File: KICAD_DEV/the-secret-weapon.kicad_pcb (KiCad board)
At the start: 6 copper layers, 100 x 100 mm, 45 parts, among them J1 USB_C_Receptacle_USB2.0_14P, J2 Screw_Terminal_01x02, U1 STM32H743VITx, U2 USBLC6-2SC6, U3 LMR33640ADDA, U4 LM1086S-3.3/TR, Y1 8 MHz, Y2 32.768 KHz

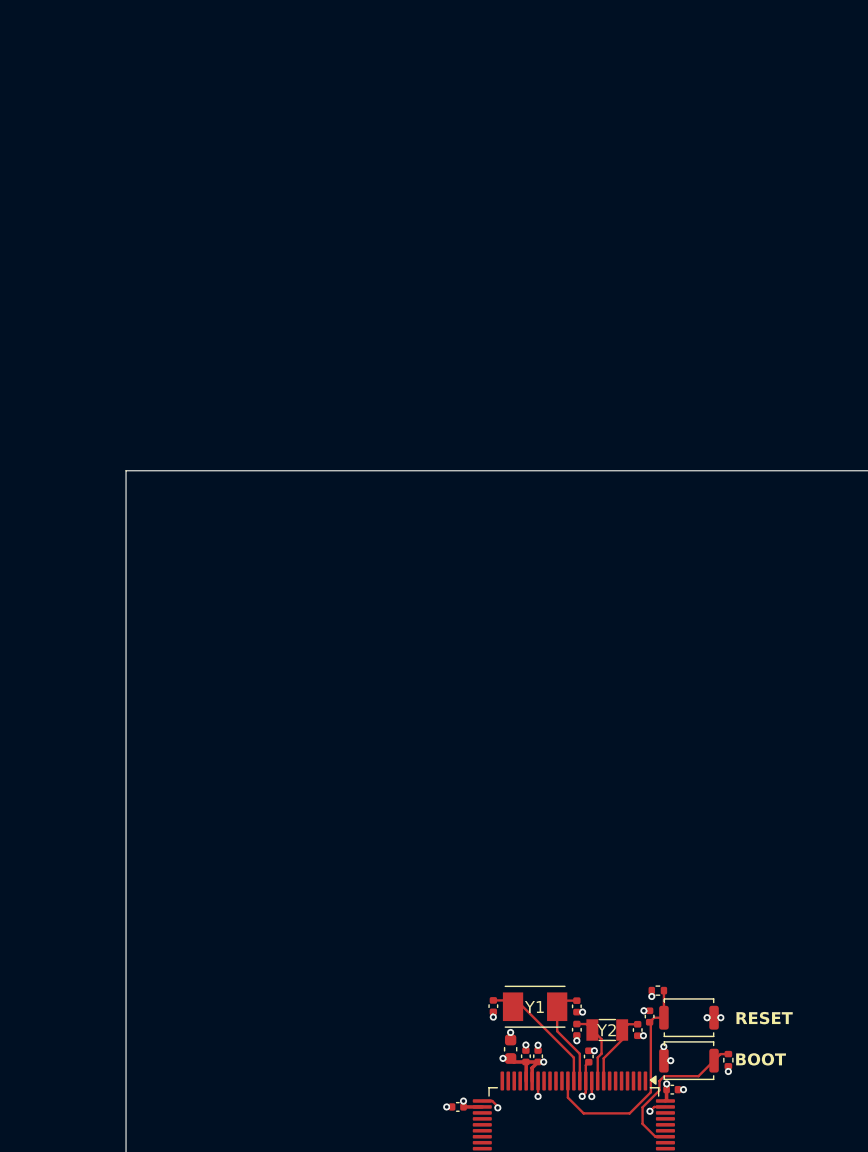
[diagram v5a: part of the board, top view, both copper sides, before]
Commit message: layed out all the components
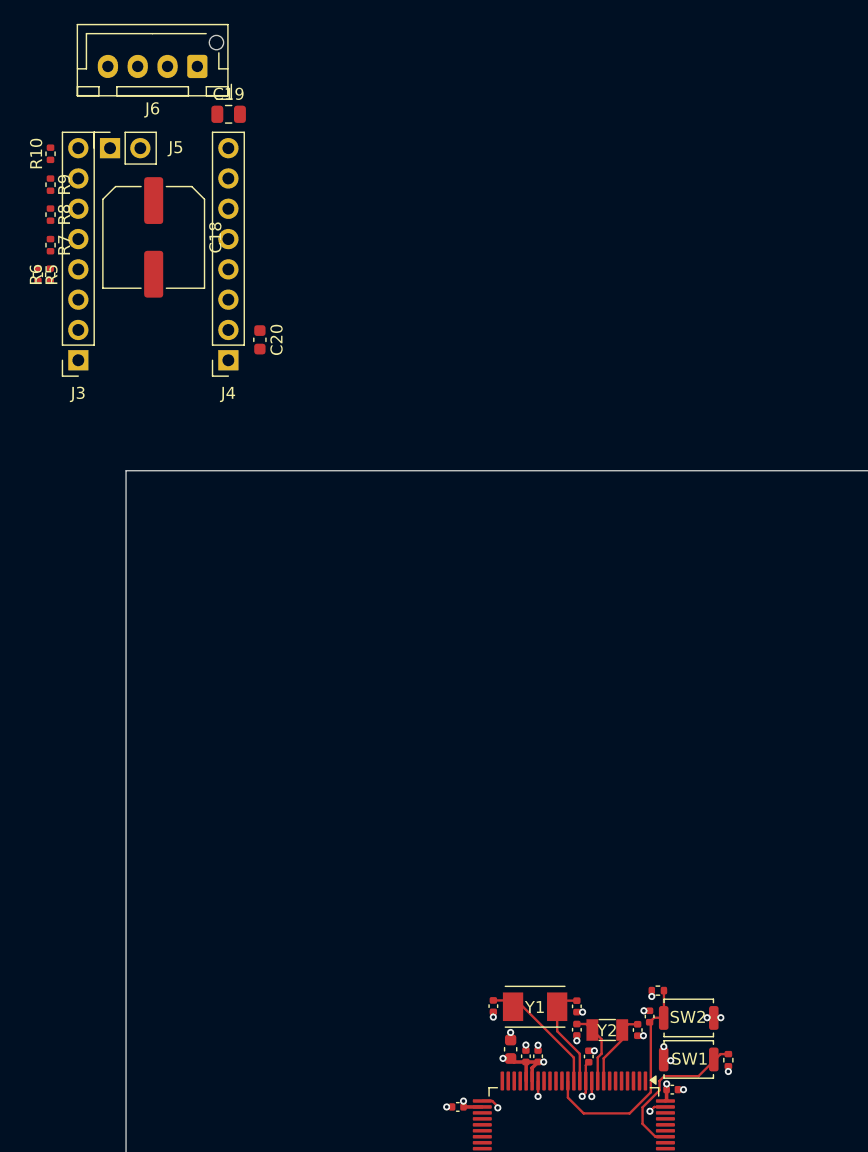
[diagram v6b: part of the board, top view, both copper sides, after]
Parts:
- removed BOOT, RESET: SW_Push, Button_Switch_SMD:SW_Push_SPST_NO_Alps_SKRK
- added C18: 220uF, Capacitor_SMD:C_Elec_8x6.2, F.Cu at (98.3, 58.9)
- added C19: 0.1uF, Capacitor_SMD:C_0805_2012Metric, F.Cu at (104.6, 48.6)
- added C20: 0.1uF, Capacitor_SMD:C_0603_1608Metric, F.Cu at (107.2, 67.5)
- added J3: Conn_01x08, Connector_PinSocket_2.54mm:PinSocket_1x08_P2.54mm_Vertical, F.Cu at (92.0, 69.2)
- added J4: Conn_01x08, Connector_PinSocket_2.54mm:PinSocket_1x08_P2.54mm_Vertical, F.Cu at (104.6, 69.2)
- added J5: Conn_01x02, Connector_PinSocket_2.54mm:PinSocket_1x02_P2.54mm_Vertical, F.Cu at (94.7, 51.5)
- added J6: Conn_01x04, Connector_JST:JST_XH_B4B-XH-AM_1x04_P2.50mm_Vertical, F.Cu at (102.0, 44.6)
- added R10: 10K, Resistor_SMD:R_0402_1005Metric, F.Cu at (89.7, 51.9)
- added R5: 1K, Resistor_SMD:R_0402_1005Metric, F.Cu at (88.6, 62.1)
- added R6: 1K, Resistor_SMD:R_0402_1005Metric, F.Cu at (89.6, 62.1)
- added R7: 10K, Resistor_SMD:R_0402_1005Metric, F.Cu at (89.7, 59.6)
- added R8: 10K, Resistor_SMD:R_0402_1005Metric, F.Cu at (89.7, 57.0)
- added R9: 10K, Resistor_SMD:R_0402_1005Metric, F.Cu at (89.7, 54.5)
- added SW1: SW_Push, Button_Switch_SMD:SW_Push_SPST_NO_Alps_SKRK, F.Cu at (143.2, 124.4)
- added SW2: SW_Push, Button_Switch_SMD:SW_Push_SPST_NO_Alps_SKRK, F.Cu at (143.2, 127.8)
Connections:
- U1 pad 28: unconnected-(U1-PA4-Pad28) -> TMC2209_DIAG
- U1 pad 29: unconnected-(U1-PA5-Pad29) -> TMC2209_INDEX
- U1 pad 30: unconnected-(U1-PA6-Pad30) -> TMC2209_EN
- U1 pad 31: unconnected-(U1-PA7-Pad31) -> TMC2209_DIR
- U1 pad 67: unconnected-(U1-PA8-Pad67) -> TMC2209_STEP
- U1 pad 68: unconnected-(U1-PA9-Pad68) -> TMC2209_TX
- U1 pad 69: unconnected-(U1-PA10-Pad69) -> TMC2209_RX

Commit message: working on routing my TMC2209 driver!
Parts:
- removed C20: 0.1uF, Capacitor_SMD:C_0603_1608Metric
- moved C19 38.8 mm to (112.7, 86.5)
- moved J3 38.8 mm to (100.1, 107.2)
- moved J4 38.8 mm to (112.6, 107.2)
- moved J5 38.8 mm to (102.7, 89.4)
- moved R10 38.8 mm to (97.7, 89.8)
- moved R5 38.8 mm to (96.7, 100.0)
- moved R6 38.8 mm to (97.7, 100.0)
- moved R9 38.8 mm to (97.7, 92.4)
- moved C18 38.8 mm to (106.4, 96.8)
- moved J6 38.8 mm to (110.0, 82.5)
- moved R7 38.8 mm to (97.7, 97.5)
- moved R8 38.8 mm to (97.7, 94.9)
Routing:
- net +12V: track 119.7 -> 127.1 mm, vias 25 -> 33
- net Net-(J3-Pin_4): track 0.00 -> 3.41 mm
- net GND: track 33.6 -> 36.5 mm, vias 73 -> 84
- net TMC2209_EN: track 0.00 -> 2.35 mm
- net Net-(J3-Pin_6): track 0.00 -> 2.34 mm
- net Net-(J3-Pin_7): track 0.00 -> 2.33 mm
- net Net-(J3-Pin_5): track 0.00 -> 2.33 mm
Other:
- board text added: "@KaiPereira's TMC2209 Stepstick!"

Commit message: finished routing my TMC2209 motor driver!
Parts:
- added C20: 0.1uF, Capacitor_SMD:C_0603_1608Metric, F.Cu at (115.3, 105.5)
- moved R5 2.09 mm to (97.7, 101.8)
- moved R6 0.20 mm to (97.7, 99.8), turned to -90 degrees
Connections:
- U1 pad 22: unconnected-(U1-PA0-Pad22) -> TMC2209_TX
- U1 pad 23: unconnected-(U1-PA1-Pad23) -> TMC2209_RX
- U1 pad 28: TMC2209_DIAG -> TMC2209_INDEX
- U1 pad 29: TMC2209_INDEX -> TMC2209_DIAG
- U1 pad 31: TMC2209_DIR -> TMC2209_STEP
- U1 pad 32: unconnected-(U1-PC4-Pad32) -> TMC2209_DIR
- U1 pad 67: TMC2209_STEP -> unconnected-(U1-PA8-Pad67)
- U1 pad 68: TMC2209_TX -> unconnected-(U1-PA9-Pad68)
- U1 pad 69: TMC2209_RX -> unconnected-(U1-PA10-Pad69)
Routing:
- net TMC2209_EN: track 2.35 -> 60.4 mm
- net TMC2209_DIAG: track 0.00 -> 56.1 mm
- net TMC2209_INDEX: track 0.00 -> 55.0 mm
- net TMC2209_TX: track 0.00 -> 53.3 mm, vias 0 -> 2
- net TMC2209_RX: track 0.00 -> 51.0 mm, vias 0 -> 2
- net TMC2209_STEP: track 0.00 -> 44.3 mm
- net TMC2209_DIR: track 0.00 -> 43.2 mm
- net Net-(J4-Pin_3): track 0.00 -> 23.7 mm
- net Net-(J4-Pin_4): track 0.00 -> 20.2 mm
- net Net-(J4-Pin_5): track 0.00 -> 16.6 mm
- net Net-(J4-Pin_6): track 0.00 -> 16.2 mm
- net +3V3: track 31.3 -> 34.5 mm, vias 39 -> 40
- net GND: track 36.5 -> 37.1 mm, vias 84 -> 85
